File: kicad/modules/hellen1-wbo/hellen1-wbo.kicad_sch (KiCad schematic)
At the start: 59 parts, among them J1 Conn_01x08, J3 Conn_01x08, J4 FTSH-107-01-F-DV-K, Q1 BTS3028, U1 MCP6004, U2 STM32F042K6Tx, U3 REF3033, U5 AD8628, U9 XC6206P332MR

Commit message: update wbo module (kicad source files)
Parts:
- removed J1, J3: Conn_01x08, Connector_PinHeader_2.54mm:PinHeader_1x08_P2.54mm_Vertical, symbol hellen1-wbo-rescue:Conn_01x08-Connector_Generic
- removed J4: FTSH-107-01-F-DV-K, Connector_PinHeader_1.27mm:PinHeader_2x07_P1.27mm_Vertical_SMD, symbol hellen1-wbo-rescue:Conn_02x07_Odd_Even-Connector_Generic
- added J1: Conn_02x03_Odd_Even, Connector:Tag-Connect_TC2030-IDC-NL_2x03_P1.27mm_Vertical, symbol Connector_Generic:Conn_02x03_Odd_Even
- added P10, P2, P3, P4, P5, P6, P7, P8, P9: Pad, footprints:MODULE-PAD-SMD_0.25x0.5, symbol hellen-one-common:Pad
- added P11, P12: Pad, footprints:MODULE-PAD-SMD_3.0, symbol hellen-one-common:Pad
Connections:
- net +3V3: now also J1.1 (Pin_1)
- net +5V: now also P2.1 (Pin_1)
- net CAN_RX: now also P5.1 (Pin_1)
- net CAN_TX: now also P6.1 (Pin_1)
- net GND: now also J1.5 (Pin_5)
- net LSU_Ip: now also P7.1 (Pin_1)
- net LSU_Rtrim: now also P9.1 (Pin_1)
- net LSU_Un: now also P10.1 (Pin_1)
- net LSU_Vm: now also P8.1 (Pin_1)
- net SWCLK: now also J1.4 (Pin_4)
- net SWDIO: now also J1.2 (Pin_2)
- net UART_RX: now also P3.1 (Pin_1)
- net UART_TX: now also P4.1 (Pin_1)
- net nRESET: now also J1.3 (Pin_3)
- net LSU_H+: now reaches Q1.2 (D)
- net LSU_H+: now also P11.1 (Pin_1)
- net LSU_H-: now reaches Q1.3 (S)
- net LSU_H-: now also P12.1 (Pin_1)
- no-connect marks 15 -> 11
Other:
- moved on the sheet: D1, Q1, R25, R27

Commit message: update wbo module kicad src
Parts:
- removed P10, P2, P3, P4, P5, P6, P7, P8, P9: Pad, footprints:MODULE-PAD-SMD_0.25x0.5, symbol hellen-one-common:Pad
- removed P11, P12: Pad, footprints:MODULE-PAD-SMD_3.0, symbol hellen-one-common:Pad
- added M600: Module-wbo-0.1, hellen-one-wbo-0.1:wbo, symbol wbo:Module-wbo-0.1
- renumbered C1 to C600, C14 to C601, C5 to C602, C3 to C603, C6 to C604, C2 to C605, C15 to C606, C4 to C607, C11 to C608, C16 to C609, C17 to C610, C7 to C611, C9 to C612, C8 to C613, C12 to C614, C13 to C615, C10 to C616, D1 to D600, D2 to D601, D3 to D602, D4 to D603, J1 to J600, Q1 to Q600, R1 to R600, R2 to R601, R31 to R602, R32 to R603, R33 to R604, R34 to R605, R9 to R606, R6 to R607, R8 to R608, R10 to R609, R16 to R610, R14 to R611, R22 to R612, R11 to R613, R12 to R614, R15 to R615, R27 to R616, R26 to R617, R3 to R618, R4 to R619, R5 to R620, R17 to R621, R25 to R622, R7 to R623, R24 to R624, R29 to R625, R30 to R626, R13 to R627, R18 to R628, U1 to U600, U5 to U601, U2 to U602, U3 to U603, U9 to U604
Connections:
- net +5V: now also M600.W1 (5V_IN)
- net CAN_RX: now also M600.W2 (CAN_RX)
- net CAN_TX: now also M600.W3 (CAN_TX)
- net GND: now also M600.G (GND)
- net LSU_H+: now also M600.E5 (LSU_H+)
- net LSU_H-: now also M600.E6 (LSU_H-)
- net LSU_Ip: now also M600.E4 (LSU_Ip)
- net LSU_Rtrim: now also M600.E2 (LSU_Rtrim)
- net LSU_Un: now also M600.E1 (LSU_Un)
- net LSU_Vm: now also M600.E3 (LSU_Vm)
- net UART_RX: no longer names the net of U602.20 (PA10)
- net UART_TX: no longer names the net of U602.19 (PA9)
- no-connect marks 11 -> 13

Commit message: update wbo
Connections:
- net +3V3: now also M600.W2 (CAN_VIO)
- net CAN_RX: now also M600.W3 (CAN_RX); no longer M600.W2 (CAN_RX)
- net CAN_TX: now also M600.W4 (CAN_TX); no longer M600.W3 (CAN_TX)
- net LSU_Ip: now also M600.E3 (LSU_Ip); no longer M600.E4 (LSU_Ip)
- net LSU_Rtrim: now also M600.E4 (LSU_Rtrim); no longer M600.E2 (LSU_Rtrim)
- net LSU_Vm: now also M600.E2 (LSU_Vm); no longer M600.E3 (LSU_Vm)
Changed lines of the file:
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@@
     (effects (font (size 1.27 1.27)) (justify left bottom))
   )
-  (label "LSU_Ip" (at 207.01 139.7 0)
+  (label "LSU_Rtrim" (at 207.01 139.7 0)
     (effects (font (size 1.27 1.27)) (justify left bottom))
   )
-  (label "LSU_Vm" (at 207.01 142.24 0)
+  (label "LSU_Ip" (at 207.01 142.24 0)
     (effects (font (size 1.27 1.27)) (justify left bottom))
   )
-  (label "LSU_Rtrim" (at 207.01 144.78 0)
+  (label "LSU_Vm" (at 207.01 144.78 0)
     (effects (font (size 1.27 1.27)) (justify left bottom))
   )
@@
     )
     (property "Datasheet" "" (id 3) (at 107.95 95.25 0)
+      (effects (font (size 1.27 1.27)) hide)
+    )
+    (pin "1")
+  )
+  (symbol (lib_id "hellen1-wbo-rescue:+3.3V-power") (at 157.48 137.16 0) (unit 1)
+    (in_bom yes) (on_board yes)
+    (property "Reference" "#PWR?" (id 0) (at 157.48 140.97 0)
+      (effects (font (size 1.27 1.27)) hide)
+    )
+    (property "Value" "+3.3V" (id 1) (at 157.861 132.7658 0))
+    (property "Footprint" "" (id 2) (at 157.48 137.16 0)
+      (effects (font (size 1.27 1.27)) hide)
+    )
+    (property "Datasheet" "" (id 3) (at 157.48 137.16 0)
       (effects (font (size 1.27 1.27)) hide)
     )
@@
     )
     (pin "E1")
+    (pin "E4")
+    (pin "W1")
+    (pin "W3")
+    (pin "G")
+    (pin "W4")
     (pin "E2")
-    (pin "W1")
-    (pin "W2")
-    (pin "G")
-    (pin "W3")
     (pin "E3")
-    (pin "E4")
     (pin "E5")
     (pin "E6")
+    (pin "W2")
   )
   (symbol (lib_id "hellen1-wbo-rescue:STM32F042K6Tx-MCU_ST_STM32F0") (at 188.595 87.63 0) (unit 1)
@@
       (reference "#PWR0649") (unit 1) (value "GND") (footprint "")
     )
+    (path "/85464752-66ec-4a65-8d45-ea14c184e4d2"
+      (reference "#PWR?") (unit 1) (value "+3.3V") (footprint "")
+    )
     (path "/00000000-0000-0000-0000-00005eb1294f"

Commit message: update wbo
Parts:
- removed M600: Module-wbo-0.1, hellen-one-wbo-0.1:wbo, symbol wbo:Module-wbo-0.1
- added M600: Module-wbo-0.1, hellen-one-wbo-0.1:wbo, symbol hellen-one-wbo-0.1:Module-wbo-0.1
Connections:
- net +3V3: now also M600.W2 (CAN_VIO)
- net +5V: now also M600.W1 (5V_IN)
- net CAN_RX: now also M600.W3 (CAN_RX)
- net CAN_TX: now also M600.W4 (CAN_TX)
- net GND: now also M600.G (GND)
- net LSU_H+: now also M600.E5 (LSU_H+)
- net LSU_H-: now also M600.E6 (LSU_H-)
- net LSU_Ip: now also M600.E3 (LSU_Ip)
- net LSU_Rtrim: now also M600.E4 (LSU_Rtrim)
- net LSU_Un: now also M600.E1 (LSU_Un)
- net LSU_Vm: now also M600.E2 (LSU_Vm)
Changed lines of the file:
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@@
     (pin "4")
   )
-  (symbol (lib_id "wbo:Module-wbo-0.1") (at 165.1 129.54 0) (unit 1)
+  (symbol (lib_id "hellen-one-wbo-0.1:Module-wbo-0.1") (at 165.1 129.54 0) (unit 1)
     (in_bom yes) (on_board yes)
     (property "Reference" "M600" (id 0) (at 181.61 125.4568 0))
@@
       (reference "J600") (unit 1) (value "Conn_02x03_Odd_Even") (footprint "Connector:Tag-Connect_TC2030-IDC-NL_2x03_P1.27mm_Vertical")
     )
-    (path "/2437dce1-e503-4c90-b344-3d1dae43121d"
+    (path "/3a3e9b13-99b4-4fcd-88a4-ee31c555ec85"
       (reference "M600") (unit 1) (value "Module-wbo-0.1") (footprint "hellen-one-wbo-0.1:wbo")
     )

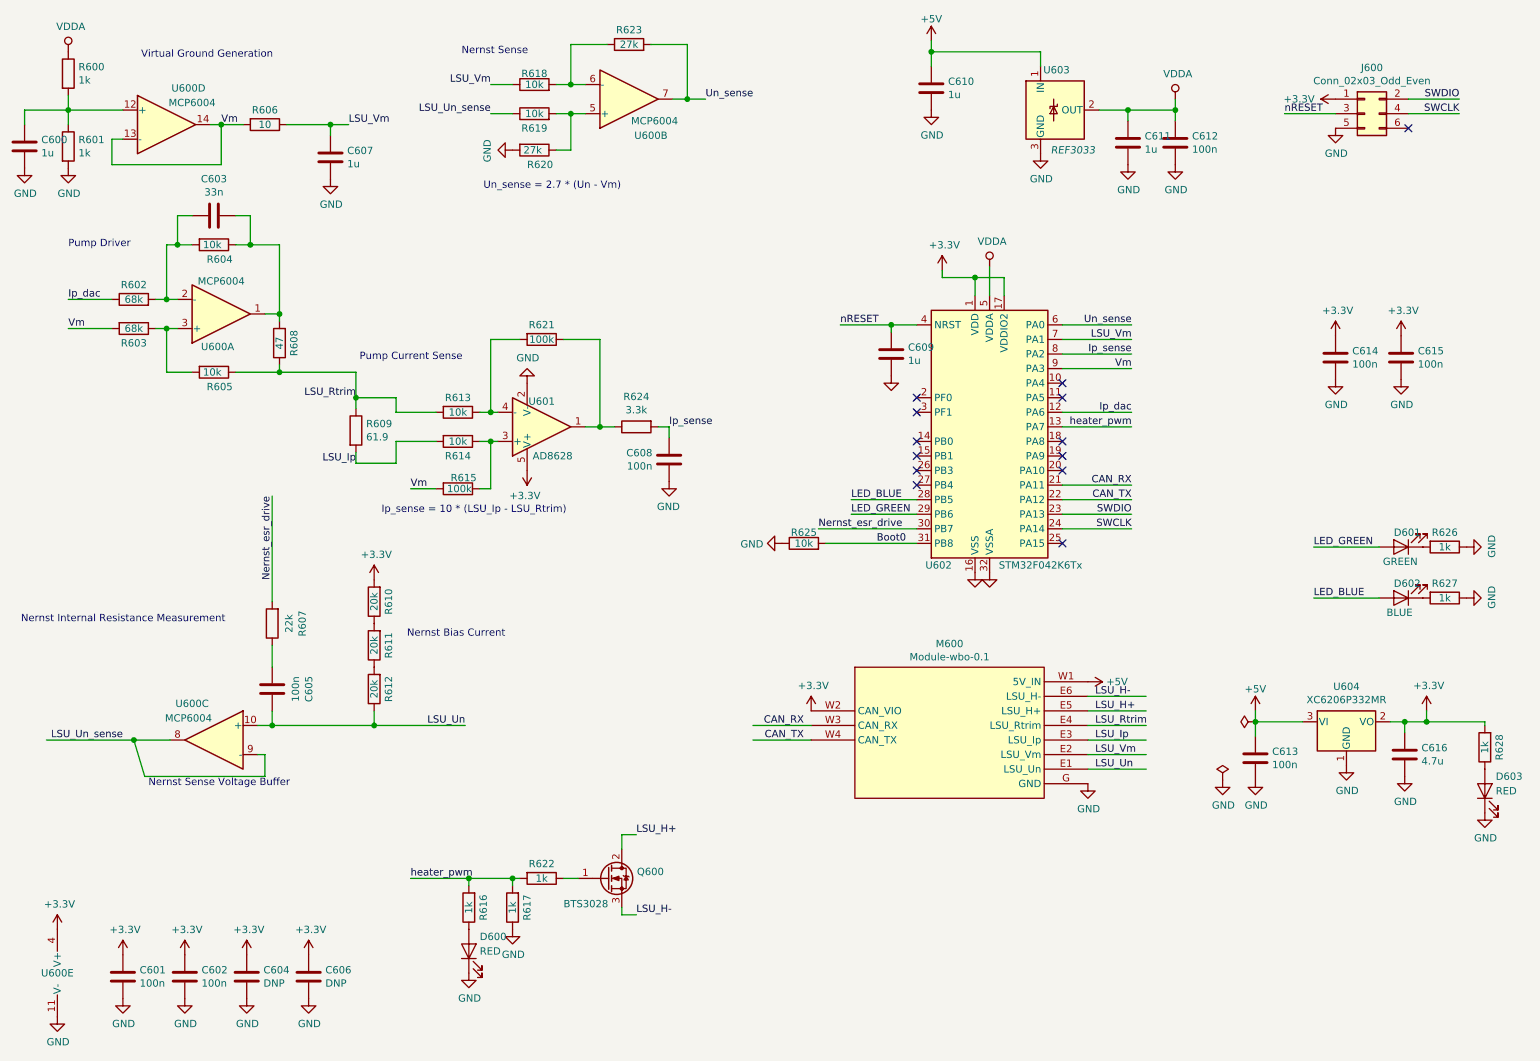
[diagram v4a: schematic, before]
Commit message: update wbo module kicad source: https://github.com/andreika-git/hellen-one/issues/13 https://github.com/andreika-git/hellen-one/issues/17
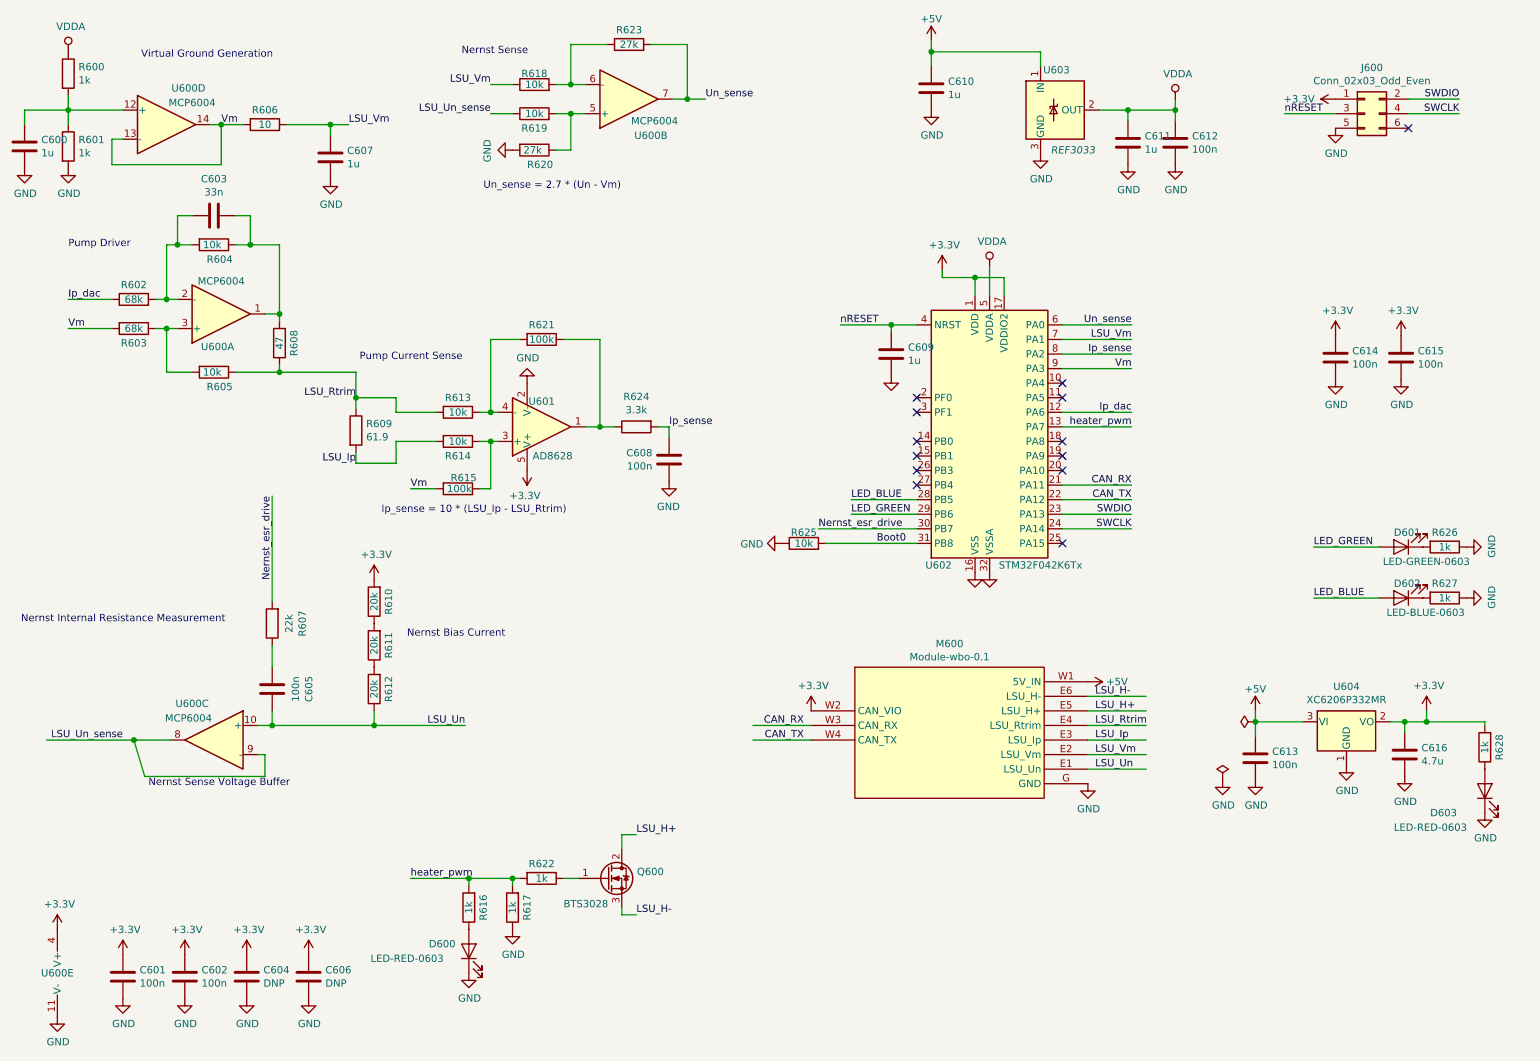
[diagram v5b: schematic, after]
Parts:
- D600, D603: value RED -> LED-RED-0603
- D601: value GREEN -> LED-GREEN-0603
- D602: value BLUE -> LED-BLUE-0603
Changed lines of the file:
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@@
   (symbol (lib_id "hellen1-wbo-rescue:LED-Device") (at 97.79 179.07 90) (unit 1)
     (in_bom yes) (on_board yes)
-    (property "Reference" "D600" (id 0) (at 99.695 176.53 90)
+    (property "Reference" "D600" (id 0) (at 90.805 177.8 90)
       (effects (font (size 1.27 1.27)) (justify right))
     )
-    (property "Value" "RED" (id 1) (at 99.695 179.07 90)
+    (property "Value" "LED-RED-0603" (id 1) (at 80.645 180.34 90)
       (effects (font (size 1.27 1.27)) (justify right))
     )
@@
       (effects (font (size 1.27 1.27)) (justify right))
     )
-    (property "Value" "GREEN" (id 1) (at 257.175 111.125 0)
+    (property "Value" "LED-GREEN-0603" (id 1) (at 257.175 111.125 0)
       (effects (font (size 1.27 1.27)) (justify right))
     )
@@
       (effects (font (size 1.27 1.27)) (justify right))
     )
-    (property "Value" "BLUE" (id 1) (at 257.81 120.015 0)
+    (property "Value" "LED-BLUE-0603" (id 1) (at 257.81 120.015 0)
       (effects (font (size 1.27 1.27)) (justify right))
     )
@@
   (symbol (lib_id "hellen1-wbo-rescue:LED-Device") (at 274.955 151.13 90) (unit 1)
     (in_bom yes) (on_board yes)
-    (property "Reference" "D603" (id 0) (at 276.86 148.59 90)
+    (property "Reference" "D603" (id 0) (at 265.43 154.94 90)
       (effects (font (size 1.27 1.27)) (justify right))
     )
-    (property "Value" "RED" (id 1) (at 276.86 151.13 90)
+    (property "Value" "LED-RED-0603" (id 1) (at 259.08 157.48 90)
       (effects (font (size 1.27 1.27)) (justify right))
     )
@@
     )
     (path "/00000000-0000-0000-0000-0000602e44ae"
-      (reference "D600") (unit 1) (value "RED") (footprint "LED_SMD:LED_0603_1608Metric")
+      (reference "D600") (unit 1) (value "LED-RED-0603") (footprint "LED_SMD:LED_0603_1608Metric")
     )
     (path "/00000000-0000-0000-0000-0000607b4b99"
-      (reference "D601") (unit 1) (value "GREEN") (footprint "LED_SMD:LED_0603_1608Metric")
+      (reference "D601") (unit 1) (value "LED-GREEN-0603") (footprint "LED_SMD:LED_0603_1608Metric")
     )
     (path "/00000000-0000-0000-0000-00005fc3f936"
-      (reference "D602") (unit 1) (value "BLUE") (footprint "LED_SMD:LED_0603_1608Metric")
+      (reference "D602") (unit 1) (value "LED-BLUE-0603") (footprint "LED_SMD:LED_0603_1608Metric")
     )
     (path "/00000000-0000-0000-0000-00005fd14734"
-      (reference "D603") (unit 1) (value "RED") (footprint "LED_SMD:LED_0603_1608Metric")
+      (reference "D603") (unit 1) (value "LED-RED-0603") (footprint "LED_SMD:LED_0603_1608Metric")
     )
     (path "/c2a04a62-ac6a-4516-8378-213e846aba4a"

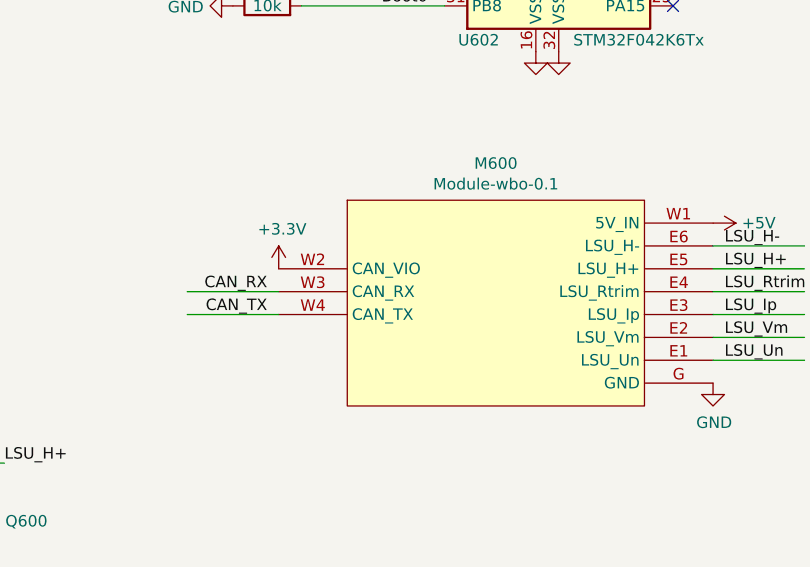
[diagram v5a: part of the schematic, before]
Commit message: wbo: add external swd pads
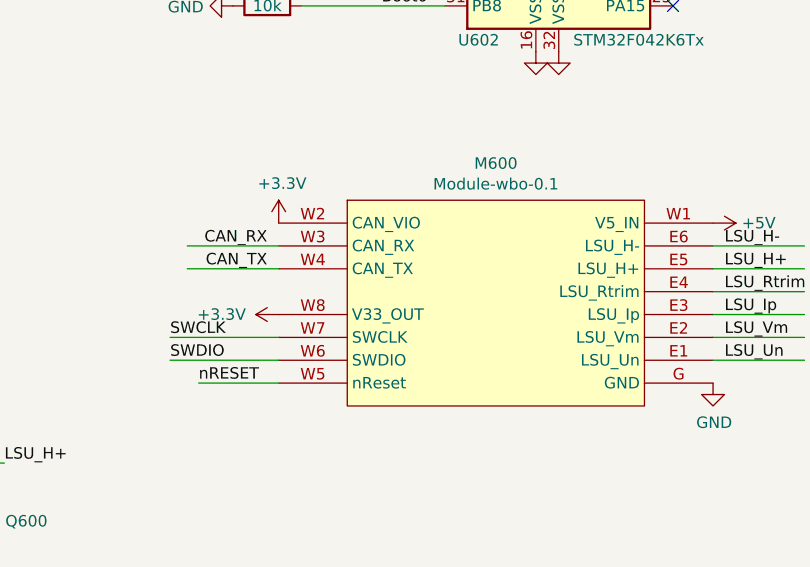
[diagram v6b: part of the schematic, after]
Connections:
- net +3V3: now also M600.W8 (V33_OUT)
- net SWCLK: now also M600.W7 (SWCLK)
- net SWDIO: now also M600.W6 (SWDIO)
- net nRESET: now also M600.W5 (nReset)

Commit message: wbo 0.2
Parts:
- removed M600: Module-wbo-0.1, hellen-one-wbo-0.1:wbo, symbol hellen-one-wbo-0.1:Module-wbo-0.1
- added M600: Module-wbo-0.2, hellen-one-wbo-0.2:wbo, symbol hellen-one-wbo-0.2:Module-wbo-0.2
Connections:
- net +3V3: now also M600.J_VCC1 (PULL_UP1), M600.J_VCC2 (PULL_UP2), M600.W2 (CAN_VIO), M600.W8 (V33_OUT)
- net +5V: now also M600.W1 (V5_IN)
- net CAN_RX: now also M600.W3 (CAN_RX)
- net CAN_TX: now also M600.W4 (CAN_TX)
- net GND: now also M600.G (GND), M600.J_GND1 (PULL_DOWN1), M600.J_GND2 (PULL_DOWN2)
- net LSU_H+: now also M600.E5 (LSU_H+)
- net LSU_H-: now also M600.E6 (LSU_H-)
- net LSU_Ip: now also M600.E3 (LSU_Ip)
- net LSU_Rtrim: now also M600.E4 (LSU_Rtrim)
- net LSU_Un: now also M600.E1 (LSU_Un)
- net LSU_Vm: now also M600.E2 (LSU_Vm)
- net SWCLK: now also M600.W7 (SWCLK)
- net SWDIO: now also M600.W6 (SWDIO)
- net nRESET: now also M600.W5 (nReset)
- net SEL1: now reaches U602.15 (PB1)
- net SEL1: now also M600.J1 (SEL1)
- net SEL2: now reaches U602.18 (PA8)
- net SEL2: now also M600.J2 (SEL2)
- no-connect marks 13 -> 11
